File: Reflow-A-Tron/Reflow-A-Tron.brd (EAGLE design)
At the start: 97.8 x 62.2 mm, 40 parts, among them IC1 ATMEGA644-10PU, J2 HOT, J3 NEUTRAL, Q1 FOXSLF/200-20, Q2 BSS123, U1 FT230X, U2 L4941BDT-TRDPAK-3, U4 MAX6675

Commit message: Fix shit
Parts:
- added R12: 10k, resistor:R0805
- moved C7 1.27 mm to (30.5, 37.1)
- moved C8 1.27 mm to (15.2, 37.1)
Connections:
- removed net GND-MCU: C6.2, C7.1, C8.1, IC1.11, IC1.31
- removed net VCC-MCU: C6.1, IC1.10, IC1.30, IC1.32
- net 5V: now also C6.1, IC1.10, IC1.30, IC1.32
- net GND: now also C6.2, C7.1, C8.1, IC1.11, IC1.31, R12.2
- net TRIAC-CTRL: now also R12.1
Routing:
- net GND-MCU: track 46.9 -> 0.00 mm, vias 1 -> 0
- net VCC-MCU: track 29.2 -> 0.00 mm
- net 5V: track 149.7 -> 178.4 mm
- net GND: track 73.4 -> 91.1 mm, vias 5 -> 10
- net NEUTRAL: track 13.6 -> 7.92 mm
- net XTAL1: track 11.5 -> 15.1 mm
- net XTAL2: track 11.6 -> 15.1 mm
- net N$9: track 44.3 -> 47.1 mm
- net N$10: track 47.4 -> 50.1 mm, vias 1 -> 2
- net MISO: track 57.4 -> 59.7 mm
- net TRIAC-CTRL: track 54.8 -> 56.4 mm
- net N$14: track 31.0 -> 31.7 mm
- net TCK: vias 4 -> 2
- added copper zone on layer 1, net GND
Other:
- board text added: "v1.1"
- board text removed: "v1.0"

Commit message: More fixes
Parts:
- moved J2 30.5 mm to (36.8, 55.9), turned to 270 degrees
- moved J3 21.6 mm to (69.8, 55.9), turned to 90 degrees
- moved JP2 5.08 mm to (10.2, 8.89)
- moved THERMOCOUPLE 2.54 mm to (83.8, 3.81)
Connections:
- net N$10 renamed RXD
- net N$9 renamed TXD
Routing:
- net 5V: track 178.4 -> 159.0 mm
- net TXD: track 47.1 -> 62.6 mm, vias 1 -> 2
- net TCK: track 27.3 -> 17.9 mm
- net TDI: track 19.4 -> 11.4 mm
- net RESET: track 73.1 -> 78.2 mm
- net HOT: track 41.5 -> 37.8 mm
- net RXD: track 50.1 -> 52.6 mm, vias 2 -> 3
- net TMS: track 12.0 -> 10.7 mm
- net TDO: track 15.6 -> 14.3 mm
- net MISO: vias 2 -> 3
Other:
- outline, holes or cut-outs redrawn
- board text added: "RXD"
- board text added: "TXD"
- board text added: "v1.2"
- board text removed: "v1.1"

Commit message: Add custom lib, still needs more work.
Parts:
- C5, C6: value 0.1uF -> 10nF; device SparkFun-Capacitors:0603-CAP -> custom:0805
- J1: device neilbetham:XM7D-0512 -> custom:XM7D-0512
- U1: device neilbetham:SSOP-16 -> custom:SSOP-16
- moved R9 7.43 mm to (40.0, 48.3), turned to 180 degrees
- moved R8 4.42 mm to (43.5, 47.3)
- moved J3 0.64 mm to (70.5, 55.9)
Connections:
- removed net ID: J1.4
- removed net MAX-SCK: IC1.8
- removed net MOSI: IC1.6
- removed net N$1: C5.1, U4.4
- removed net N$2: IC1.5
- net 5V: now also C5.1, U4.4
- net CS: now also IC1.5
- net SCK: now also IC1.8
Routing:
- net SCK: track 3.87 -> 83.6 mm, vias 0 -> 2
- net CS: track 8.72 -> 70.1 mm, vias 0 -> 2
- net N$15: track 23.0 -> 13.9 mm
- net GND: track 91.1 -> 99.5 mm
- net N$3: track 7.07 -> 13.5 mm
- net N$14: track 31.7 -> 26.1 mm, vias 0 -> 1
- net 5V: track 159.0 -> 154.5 mm, vias 5 -> 4
- net N$12: track 8.01 -> 3.76 mm
- net N$1: track 3.63 -> 0.00 mm
- net HOT: track 37.8 -> 40.6 mm
- net NEUTRAL: track 7.92 -> 9.45 mm, vias 2 -> 0
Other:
- board text added: "MISO"
- board text added: "v1.3"
- board text removed: "v1.2"

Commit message: Next rev with more bug fixes
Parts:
- moved C3 4.62 mm to (76.2, 25.7), turned to 90 degrees
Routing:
- net GND: track 99.5 -> 57.8 mm, vias 10 -> 13
- net 5V: track 154.5 -> 193.0 mm, vias 4 -> 6
- net SCK: track 83.6 -> 72.5 mm
- net N$14: track 26.1 -> 25.0 mm, vias 1 -> 2
- net N$3: track 13.5 -> 14.0 mm, vias 0 -> 1
- added copper zone on layer 16, net HOT
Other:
- board text added: "v1.4"
- board text removed: "v1.3"

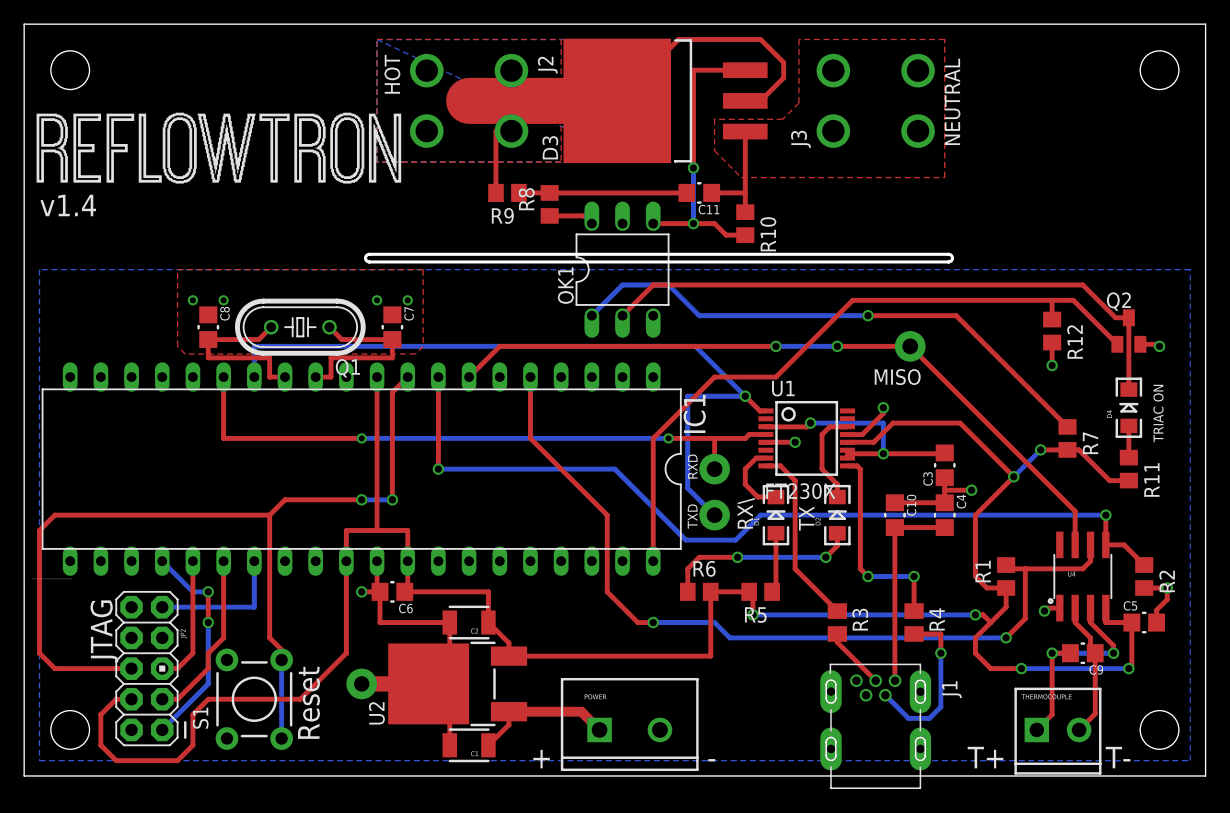
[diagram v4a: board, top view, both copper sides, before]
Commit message: Hardware Working for reflow a tron
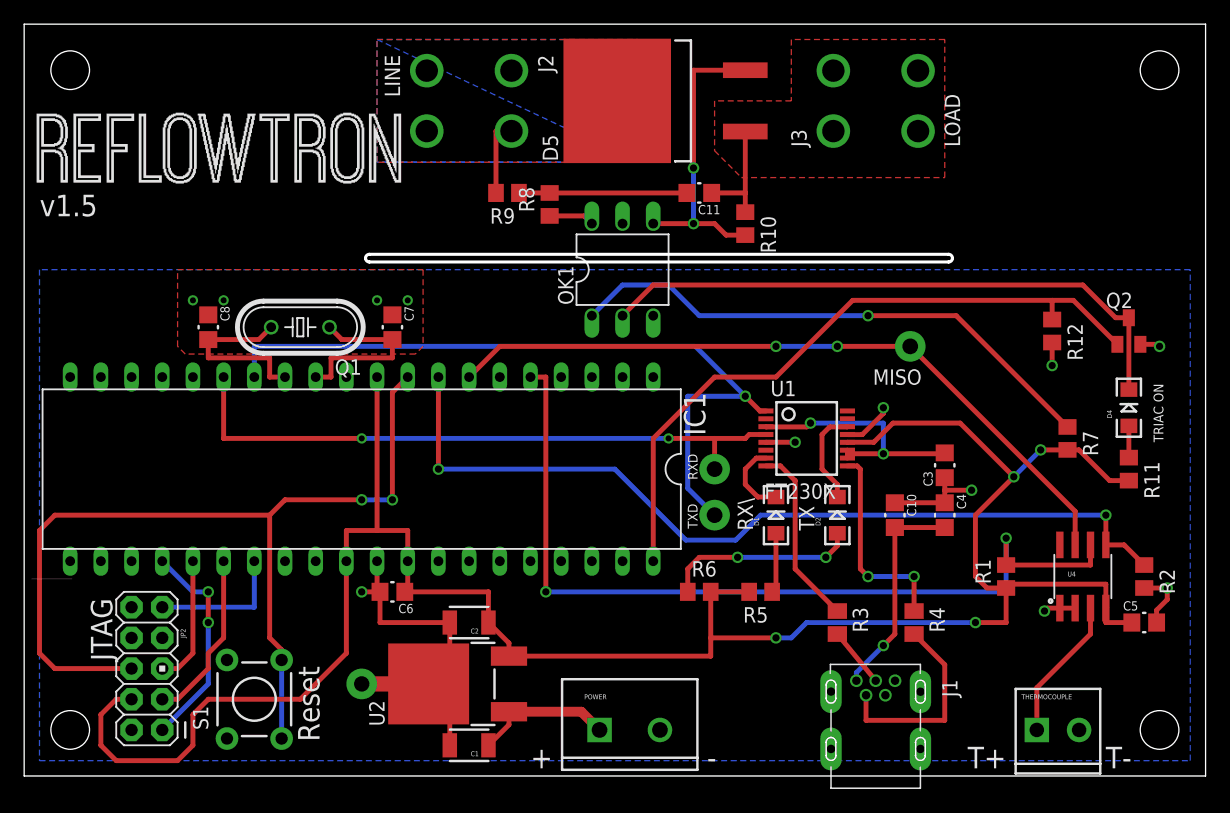
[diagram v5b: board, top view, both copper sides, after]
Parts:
- removed C9: 10nF, neilbetham:0805
- removed D3: (no value), neilbetham:D2PAK
- added D5: HV TRIAC, custom:D2PAK
- C5: value 10nF -> 100nF
- J1: value (none) -> USB Mini
- J2: value HOT -> LINE
- J3: value NEUTRAL -> LOAD
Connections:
- removed net T-: C9.1, THERMOCOUPLE.2, U4.2
- net GND: now also THERMOCOUPLE.2, U4.2
- net HOT: now also D5.4; no longer D3.2, D3.4
- net N$14: now also D5.3; no longer D3.3
- net NEUTRAL: now also D5.1; no longer D3.1
- net T+: no longer C9.2
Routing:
- net HOT: track 40.6 -> 6.40 mm
- net T-: track 11.3 -> 0.00 mm
- net 5V: track 193.0 -> 185.1 mm, vias 6 -> 4
- net T+: track 18.0 -> 11.9 mm, vias 2 -> 0
- net N$3: track 14.0 -> 16.8 mm, vias 1 -> 0
- net CS: track 70.1 -> 72.5 mm
- net USB-VCC: track 16.8 -> 18.1 mm, vias 0 -> 1
- net GND: track 57.8 -> 59.0 mm
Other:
- board text added: "v1.5"
- board text removed: "v1.4"
